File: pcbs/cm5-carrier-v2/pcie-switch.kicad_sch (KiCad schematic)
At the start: 94 parts, among them U1001 SYA75603A, U1002 PCI11010C, U1003 AT24C64D-MAHM-E, Y1001 XRCGB25M000F3A16R0

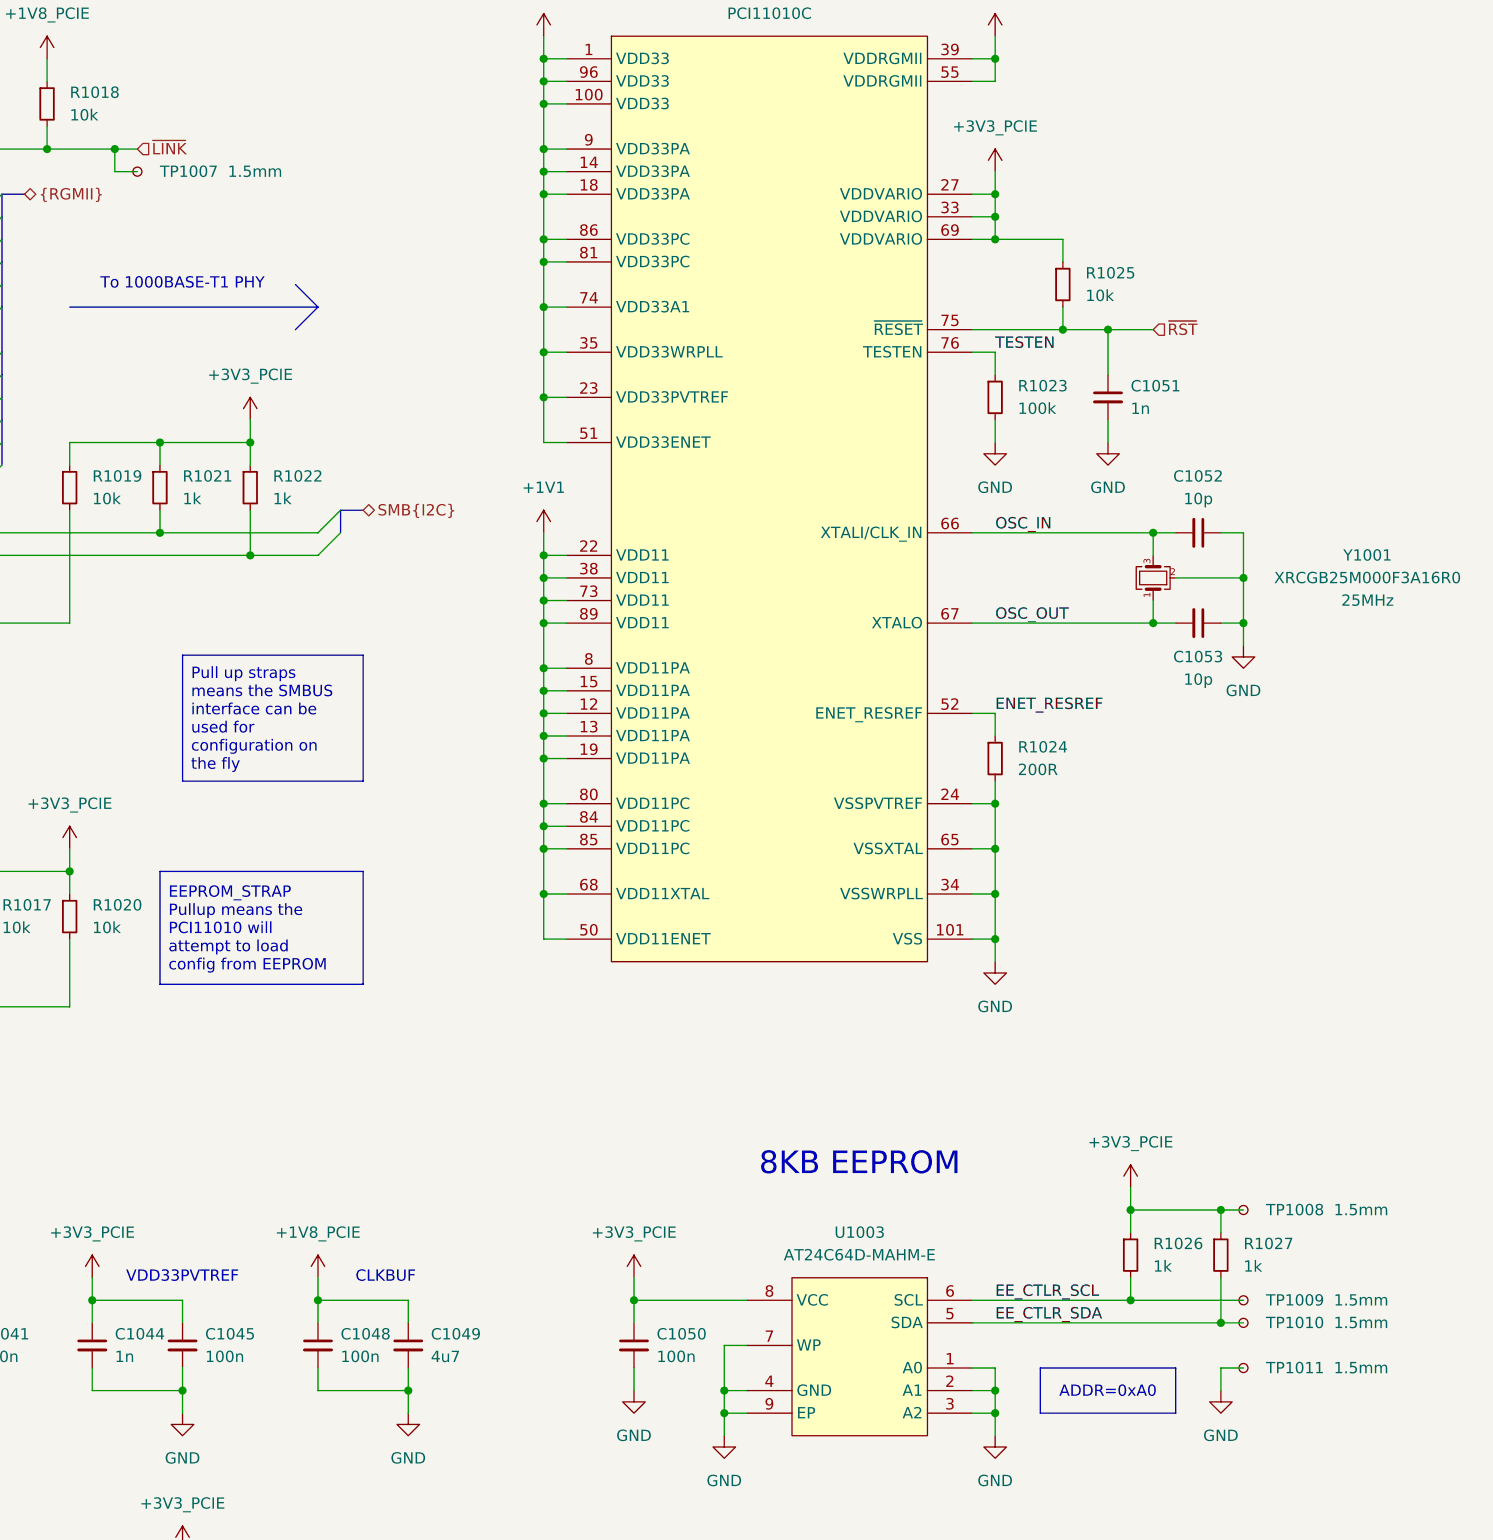
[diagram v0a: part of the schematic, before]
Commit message: Changed UART connector to I2C
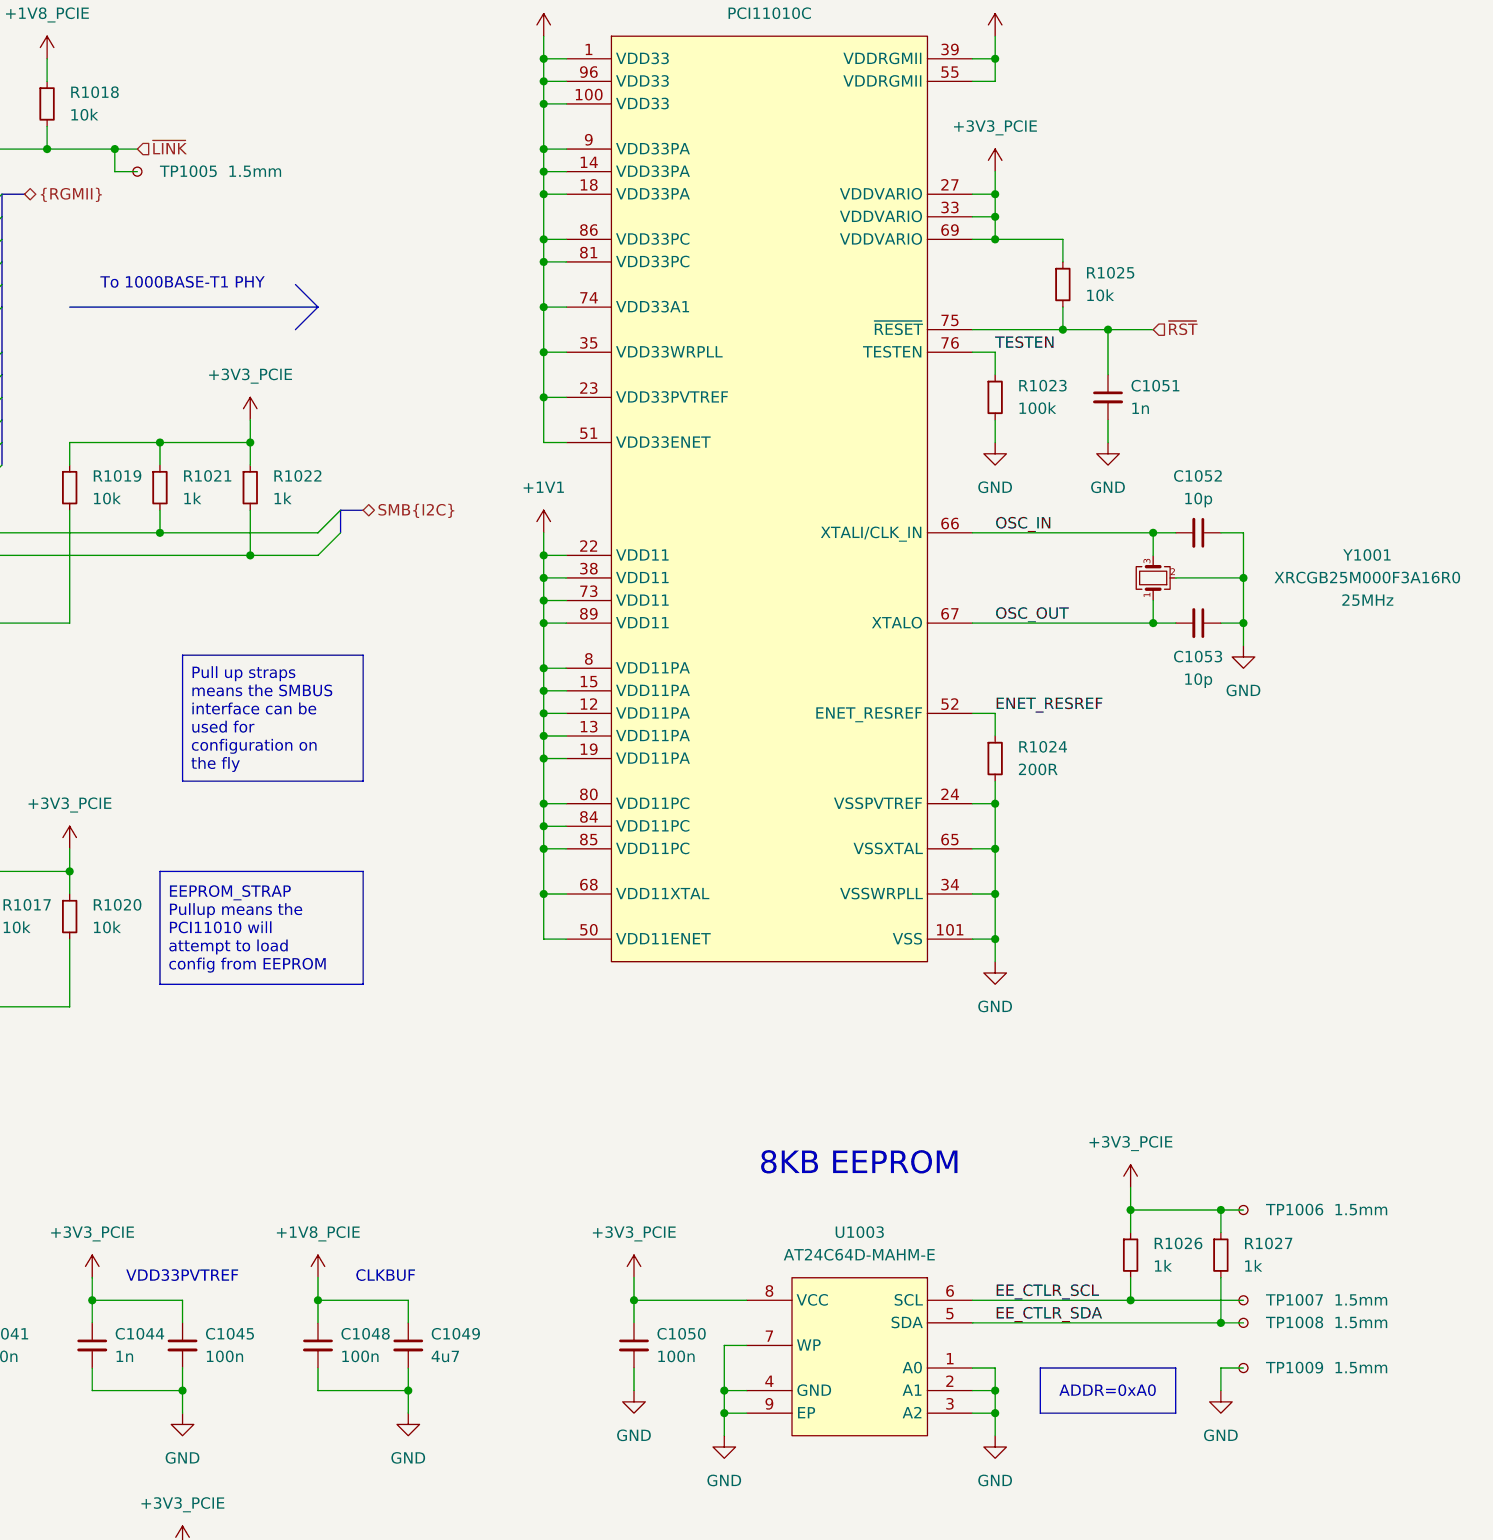
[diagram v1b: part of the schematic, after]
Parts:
- renumbered TP1007 to TP1005, TP1008 to TP1006, TP1009 to TP1007, TP1010 to TP1008, TP1011 to TP1009
